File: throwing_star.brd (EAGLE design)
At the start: 53.3 x 53.3 mm, 6 parts

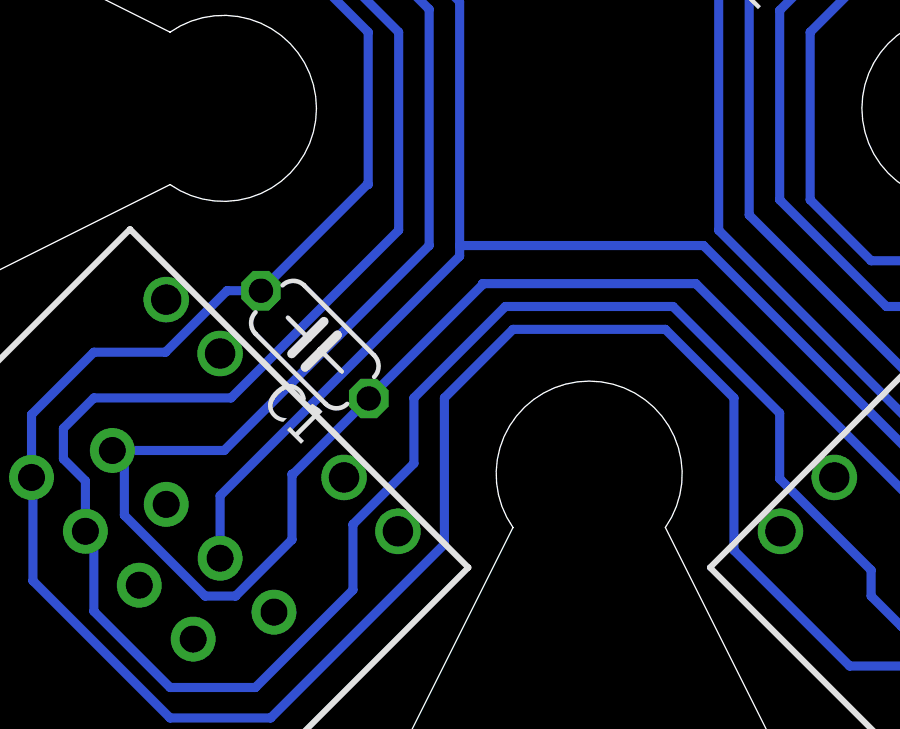
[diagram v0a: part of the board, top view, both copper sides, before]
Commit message: adjust text, add logo
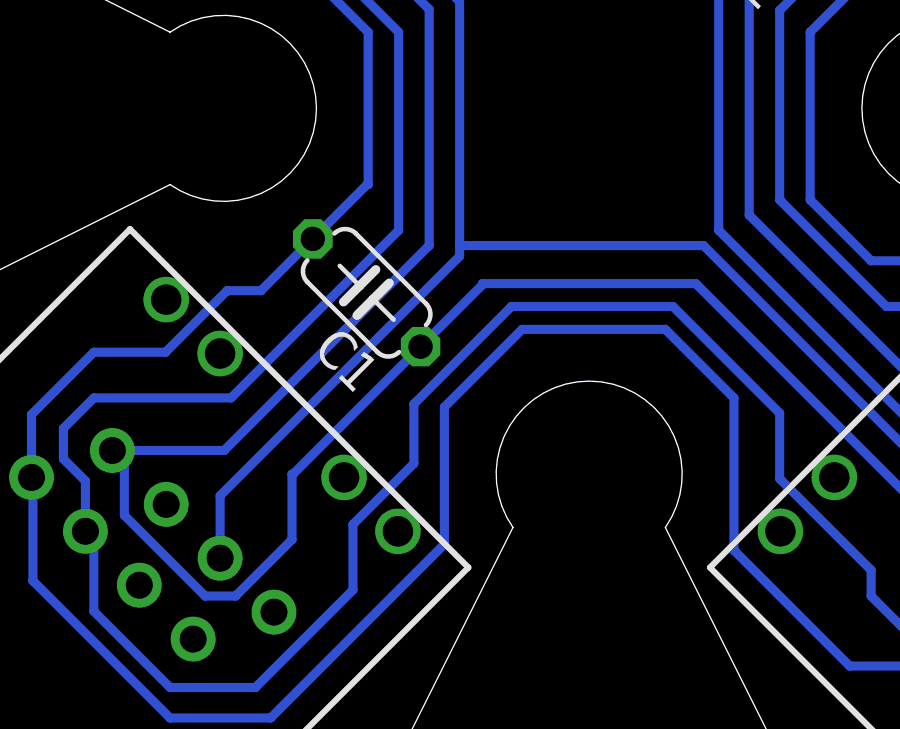
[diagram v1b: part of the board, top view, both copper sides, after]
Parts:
- moved C1 2.44 mm to (16.7, 49.7)
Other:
- board text added: "Star"
- board text added: "Throwing"
- board text removed: "NETZ39 Throwing Star"

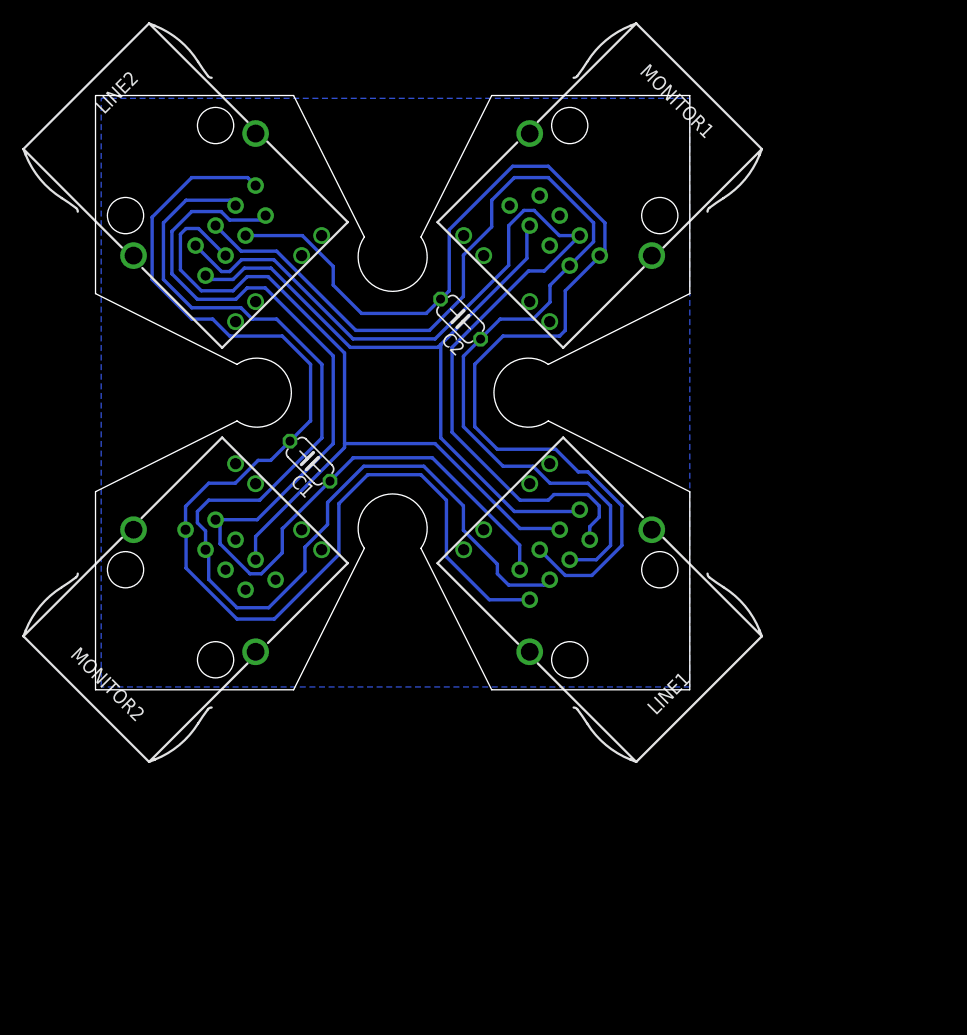
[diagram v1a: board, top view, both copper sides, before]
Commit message: condense to ~50x50mm
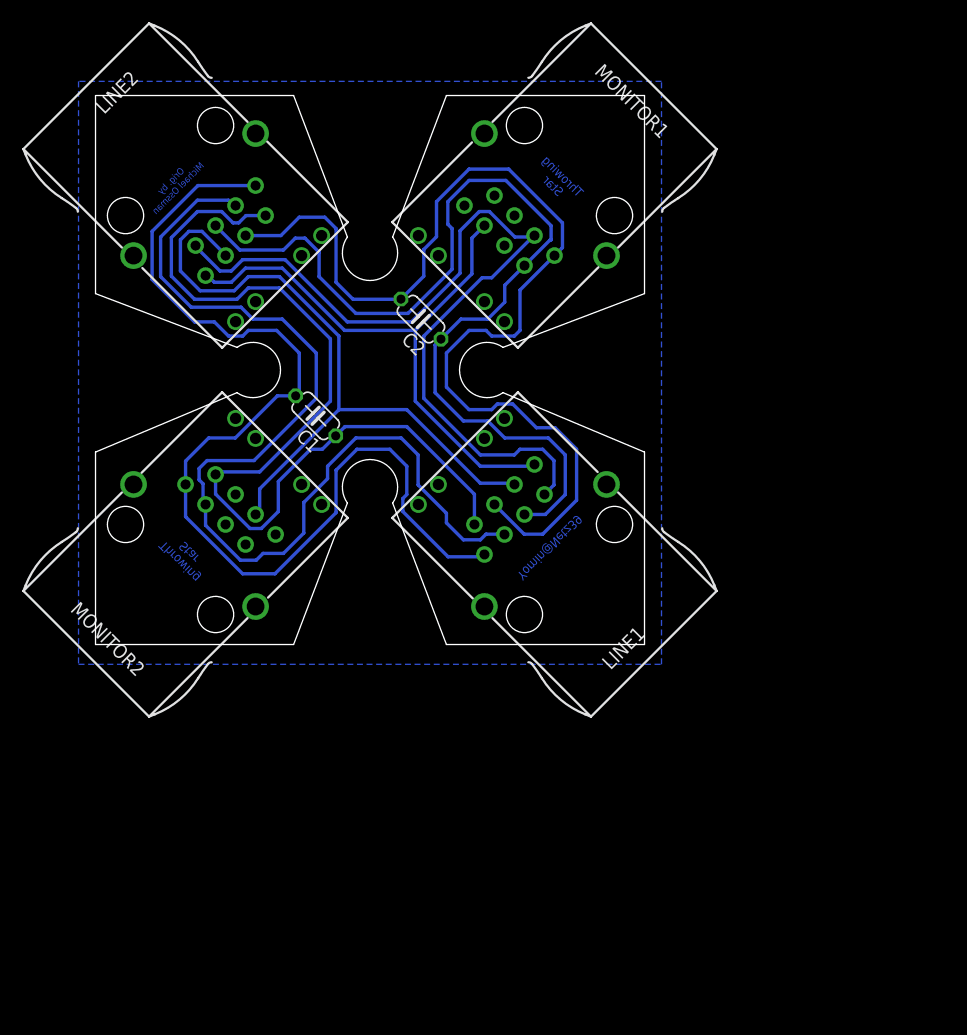
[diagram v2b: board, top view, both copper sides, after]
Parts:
- moved LINE1 5.75 mm to (37.8, 42.2)
- moved C1 4.10 mm to (17.2, 53.8)
- moved MONITOR1 4.06 mm to (37.8, 73.7)
- moved MONITOR2 4.06 mm to (6.35, 42.2)
- moved C2 3.56 mm to (26.7, 62.5)
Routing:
- net 8: track 107.5 -> 95.7 mm
- net 2: track 89.6 -> 78.6 mm
- net 6: track 102.8 -> 92.2 mm
- net 1: track 62.4 -> 53.4 mm
- net 4: track 97.5 -> 89.0 mm
- net 3: track 71.7 -> 63.5 mm
- net 7: track 94.5 -> 86.5 mm
- net 5: track 102.2 -> 96.0 mm
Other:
- board size 53.3 x 53.3 mm -> 49.3 x 49.3 mm
- board text added: "Throwing Star"
- board text removed: "Great Scott Gadgets"
- board text removed: "Star"
- board text removed: "Throwing"

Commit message: change rj45 jacks and reroute
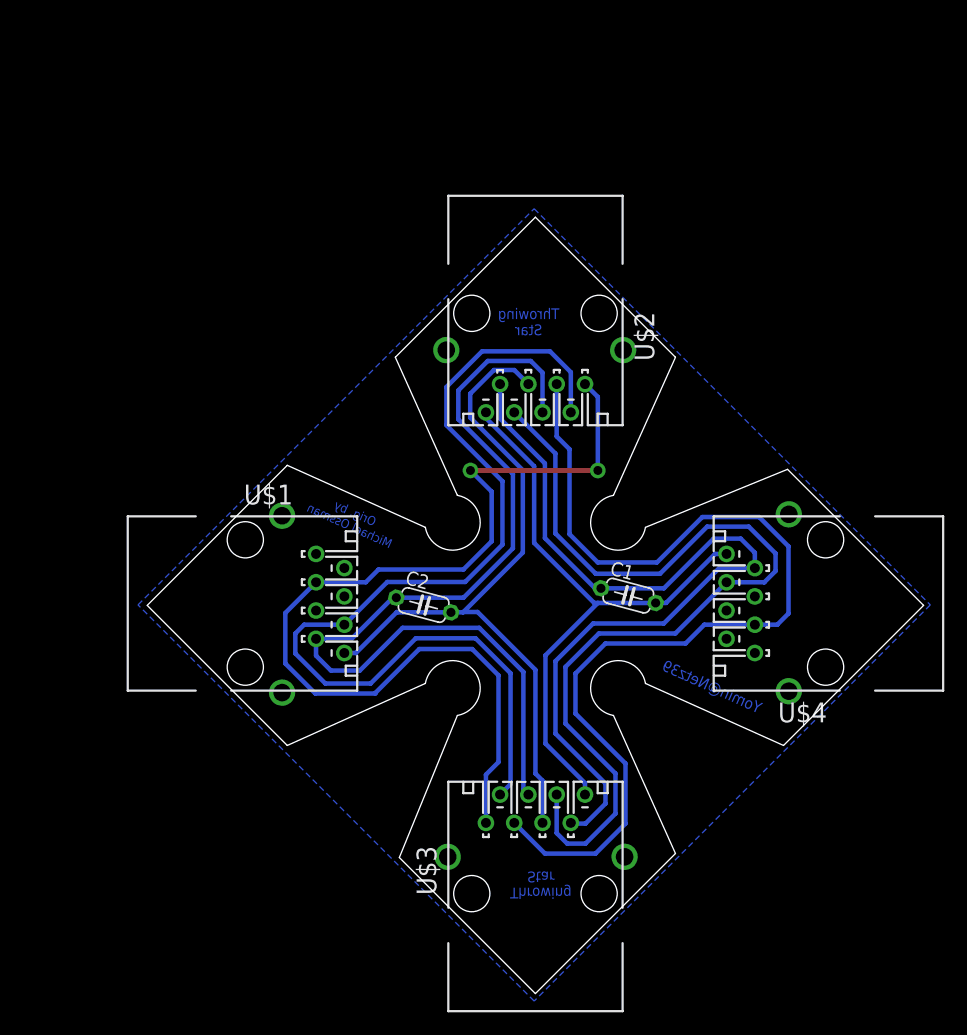
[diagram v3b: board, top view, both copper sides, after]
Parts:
- removed LINE1, LINE2, MONITOR1, MONITOR2: SI-50170, con-stewart:SI-50170
- added U$1, U$2, U$3, U$4: RJ45MOD, con-appsys:RJ45MOD
- moved C1 32.4 mm to (45.3, 37.7), turned to 345 degrees
- moved C2 25.7 mm to (26.9, 36.8), turned to 345 degrees
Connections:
- net 1: now also U$1.3, U$2.1, U$3.1; no longer LINE1.1, LINE2.1, MONITOR1.3
- net 2: now also U$1.6, U$2.2, U$3.2; no longer LINE1.2, LINE2.2, MONITOR1.6
- net 3: now also U$2.3, U$3.3, U$4.3; no longer LINE1.3, LINE2.3, MONITOR2.3
- net 4: now also U$1.7, U$2.4, U$3.4; no longer LINE1.4, LINE2.4, MONITOR1.7
- net 5: now also U$1.8, U$2.5, U$3.5; no longer LINE1.5, LINE2.5, MONITOR1.8
- net 6: now also U$2.6, U$3.6, U$4.6; no longer LINE1.6, LINE2.6, MONITOR2.6
- net 7: now also U$2.7, U$3.7, U$4.7; no longer LINE1.7, LINE2.7, MONITOR2.7
- net 8: now also U$2.8, U$3.8, U$4.8; no longer LINE1.8, LINE2.8, MONITOR2.8
- net GND: now also U$1.G3, U$1.G4, U$2.G3, U$2.G4, U$3.G3, U$3.G4, U$4.G3, U$4.G4; no longer LINE1.S1, LINE1.S2, LINE2.S1, LINE2.S2, MONITOR1.S1, MONITOR1.S2, MONITOR2.S1, MONITOR2.S2
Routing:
- net 8: track 95.7 -> 55.4 mm
- net 1: track 53.4 -> 89.1 mm, vias 0 -> 2
- net 5: track 96.0 -> 65.2 mm
- net 3: track 63.5 -> 92.4 mm
- net 2: track 78.6 -> 91.5 mm
- net 7: track 86.5 -> 79.8 mm
- net 6: track 92.2 -> 85.7 mm
- net 4: track 89.0 -> 85.0 mm
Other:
- board size 49.3 x 49.3 mm -> 69.7 x 69.7 mm
